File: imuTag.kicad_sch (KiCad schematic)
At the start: 33 parts, among them J1 Conn_02x05_Odd_Even, J2 Conn_01x04_Pin, J3 Conn_01x02_Pin, Q1 DMG2305UX-13, U1 E73-2G4M08S1C, U2 ME6211C30M5G-N, U3 GD25Q64ESIG, Y2 Crystal

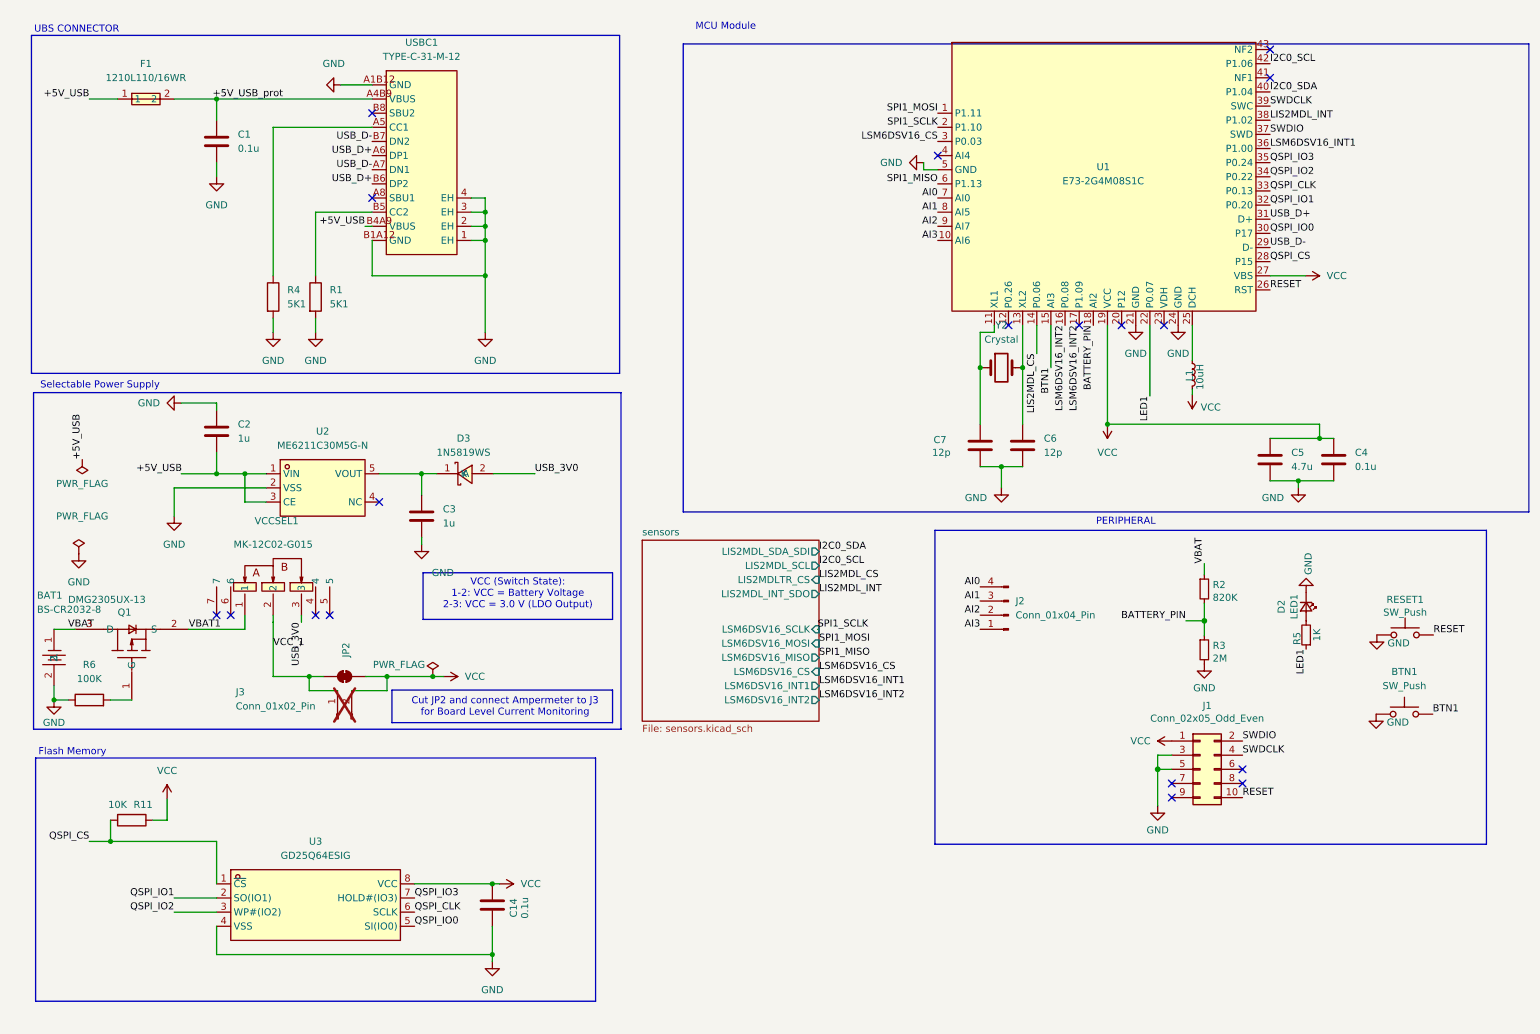
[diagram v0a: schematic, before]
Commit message: feat: imuTag mini PCBA v1.0 – initial release
PCB layout, schematics (imuTag + sensors), custom EasyEDA symbol/footprint libraries with 3D models, design rules, and production outputs (BOM, placement, netlist).
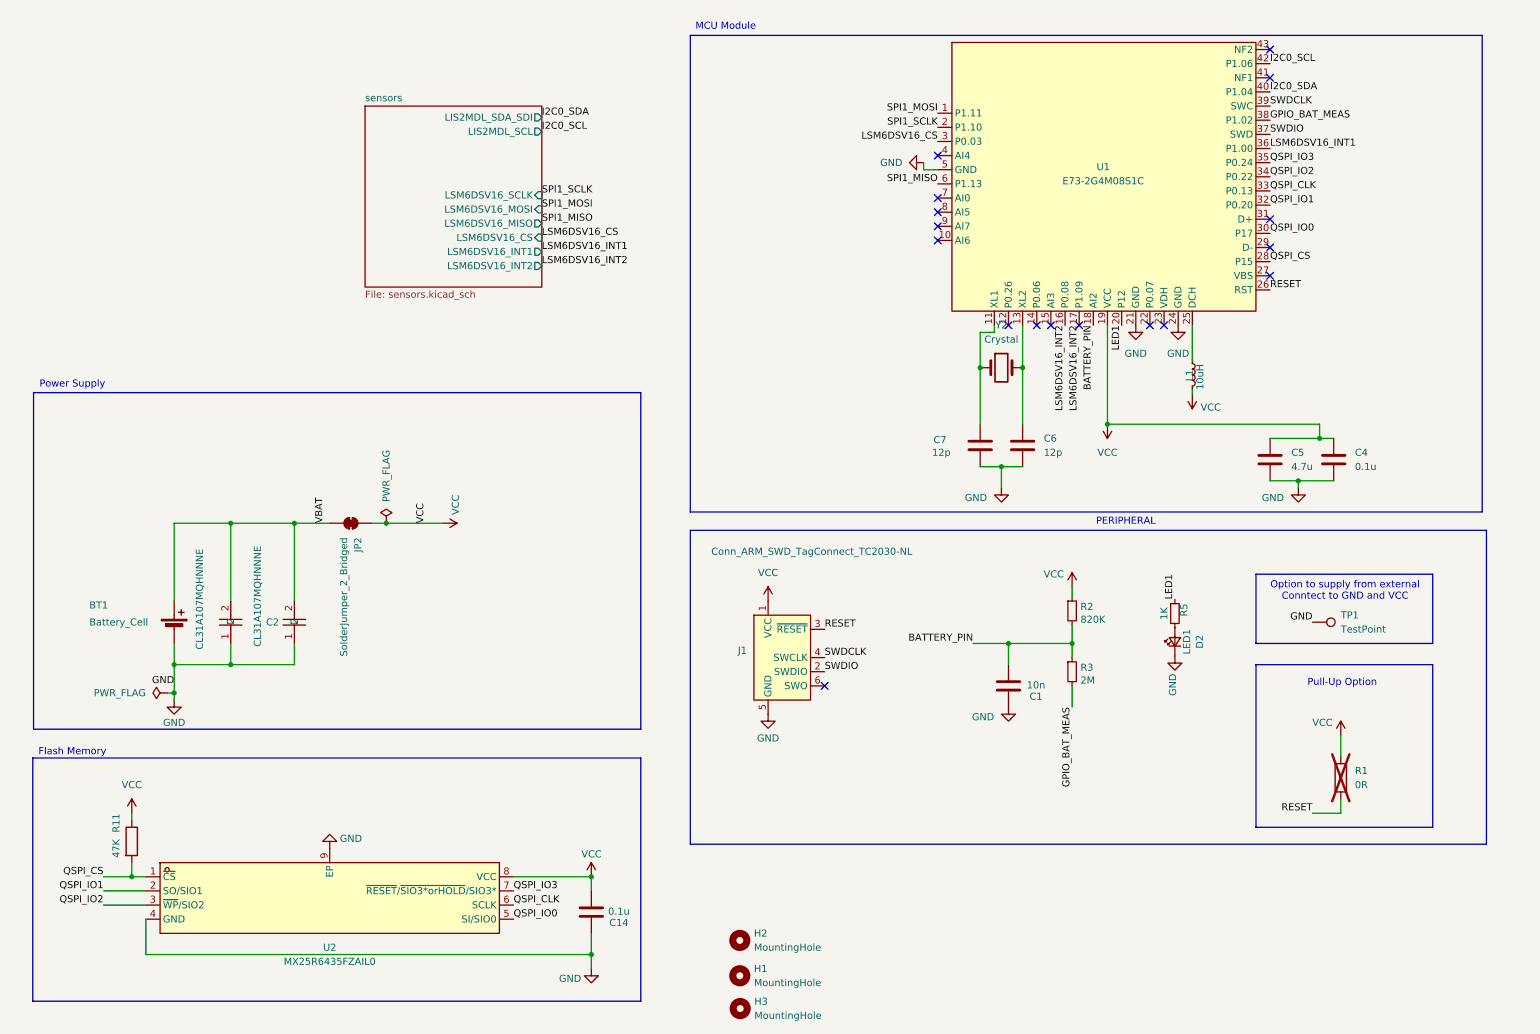
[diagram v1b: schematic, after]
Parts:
- removed BAT1: BS-CR2032-8, EasyEDA:BAT-TH_MY-2032-22, symbol EasyEDA:BS-CR2032-8
- removed BTN1, RESET1: SW_Push, EasyEDA:SW-SMD_TS-1086EV-AR03526, symbol Switch:SW_Push
- removed C2, C3: 1u, Capacitor_SMD:C_0603_1608Metric, symbol Device:C
- removed D3: 1N5819WS, EasyEDA:SOD-323_L1.8-W1.3-LS2.5-RD, symbol EasyEDA:1N5819WS
- removed F1: 1210L110/16WR, EasyEDA:F1210, symbol EasyEDA:1210L110_16WR
- removed J1: Conn_02x05_Odd_Even, Connector_PinHeader_1.27mm:PinHeader_2x05_P1.27mm_Vertical_SMD, symbol Connector_Generic:Conn_02x05_Odd_Even
- removed J2: Conn_01x04_Pin, Connector_PinHeader_2.54mm:PinHeader_1x04_P2.54mm_Vertical, symbol Connector:Conn_01x04_Pin
- removed J3: Conn_01x02_Pin, Connector_PinSocket_2.54mm:PinSocket_1x02_P2.54mm_Vertical, symbol Connector:Conn_01x02_Pin
- removed Q1: DMG2305UX-13, EasyEDA:SOT-23-3_L2.9-W1.3-P1.90-LS2.4-BR, symbol EasyEDA:DMG2305UX-13
- removed R4: 5K1, Resistor_SMD:R_0402_1005Metric, symbol Device:R
- removed R6: 100K, Resistor_SMD:R_0402_1005Metric, symbol Device:R
- removed U2: ME6211C30M5G-N, EasyEDA:SOT-23-5_L2.9-W1.6-P0.95-LS2.8-BL, symbol EasyEDA:ME6211C30M5G-N
- removed U3: GD25Q64ESIG, EasyEDA:SOP-8_L5.3-W5.3-P1.27-LS8.0-BL, symbol EasyEDA:GD25Q64ESIG
- removed USBC1: TYPE-C-31-M-12, EasyEDA:USB-C_SMD-TYPE-C-31-M-12_1, symbol EasyEDA:TYPE-C-31-M-12
- removed VCCSEL1: MK-12C02-G015, EasyEDA:SW-SMD_G-SWITCH_MK-12C02-G015, symbol EasyEDA:MK-12C02-G015
- added BT1: Battery_Cell, EasyEDA:CR2032_Custom_Contacts_SMD_AirTagStyle, symbol Device:Battery_Cell
- added C2, C8: CL31A107MQHNNNE, EasyEDA:C1206, symbol EASYEDA:CL31A107MQHNNNE
- added H1, H3: MountingHole, MountingHole:MountingHole_2.1mm, symbol Mechanical:MountingHole
- added H2: MountingHole, EasyEDA:Slot_1.2x3.0mm_NPTH, symbol Mechanical:MountingHole
- added J1: Conn_ARM_SWD_TagConnect_TC2030-NL, Connector:Tag-Connect_TC2030-IDC-NL_2x03_P1.27mm_Vertical, symbol Connector:Conn_ARM_SWD_TagConnect_TC2030-NL
- added TP1: TestPoint, TestPoint:TestPoint_Pad_D1.0mm, symbol Connector:TestPoint
- added U2: MX25R6435FZAIL0, EasyEDA:WSON-8_L4.0-W4.0-P0.80-BL-EP-1, symbol EasyEDA:MX25R6435FZAIL0
- C1: value 0.1u -> 10n
- JP2: footprint Jumper:SolderJumper-2_P1.3mm_Bridged_Pad1.0x1.5mm -> Jumper:SolderJumper-2_P1.3mm_Bridged2Bar_Pad1.0x1.5mm
- R1: value 5K1 -> 0R; footprint Resistor_SMD:R_0402_1005Metric -> Resistor_SMD:R_0805_2012Metric_Pad1.20x1.40mm_HandSolder; now not fitted
- R11: value 10K -> 47K
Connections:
- net +5V_USB_prot is gone; now on net GND: C1.1
- net VCC_1 is gone; now on net VCC: JP2.2 (B)
- net BATTERY_PIN: now also C1.2
- net GND: now also BT1.2 (-), C2.1, C8.1, J1.5 (GND), TP1.1, U2.4 (GND), U2.9 (EP); no longer C1.2, R1.2, R3.2
- net LED1: now also U1.20 (P12); no longer U1.22 (P0.07)
- net QSPI_CLK: now also U2.6 (SCLK)
- net QSPI_CS: now also U2.1 (~{CS})
- net QSPI_IO0: now also U2.5 (SI/SIO0)
- net QSPI_IO1: now also U2.2 (SO/SIO1)
- net QSPI_IO2: now also U2.3 (~{WP}/SIO2)
- net QSPI_IO3: now also U2.7 (~{RESET}/~{SIO3*orHOLD}/SIO3*)
- net RESET: now also R1.2, J1.3 (~{RESET})
- net SWDCLK: now also J1.4 (SWCLK)
- net SWDIO: now also J1.2 (SWDIO)
- net VBAT: now also JP2.1 (A), BT1.1 (+), C2.2, C8.2; no longer R2.1
- net VCC: now also R1.1, R2.1, J1.1 (VCC), U2.8 (VCC); no longer JP2.1 (A), U1.27 (VBS)
- net AI0: no longer names the net of U1.7 (AI0)
- net AI1: no longer names the net of U1.8 (AI5)
- net AI2: no longer names the net of U1.9 (AI7)
- net AI3: no longer names the net of U1.10 (AI6)
- net BTN1: no longer names the net of U1.15 (AI3)
- net LIS2MDL_CS: no longer names the net of U1.14 (P0.06)
- net LIS2MDL_INT renamed GPIO_BAT_MEAS
- net GPIO_BAT_MEAS: now also R3.2
- net USB_D+: no longer names the net of U1.31 (D+)
- net USB_D-: no longer names the net of U1.29 (D-)
- no-connect marks 18 -> 17
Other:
- sheet sensors ports: added none; removed LIS2MDLTR_CS, LIS2MDL_INT_SDO
- note added: "Option to supply from external Conntect to GND and VCC"
- note added: "Power Supply"
- note added: "Pull-Up Option"
- note removed: "Cut JP2 and connect Ampermeter to J3 for Board Level Current Monitoring"
- note removed: "Selectable Power Supply"
- note removed: "UBS CONNECTOR"
- note removed: "VCC (Switch State): 1-2: VCC = Battery Voltage 2-3: VCC = 3.0 V (LDO Output)"
- moved on the sheet: C14, D2, R11, R2, R3, R5

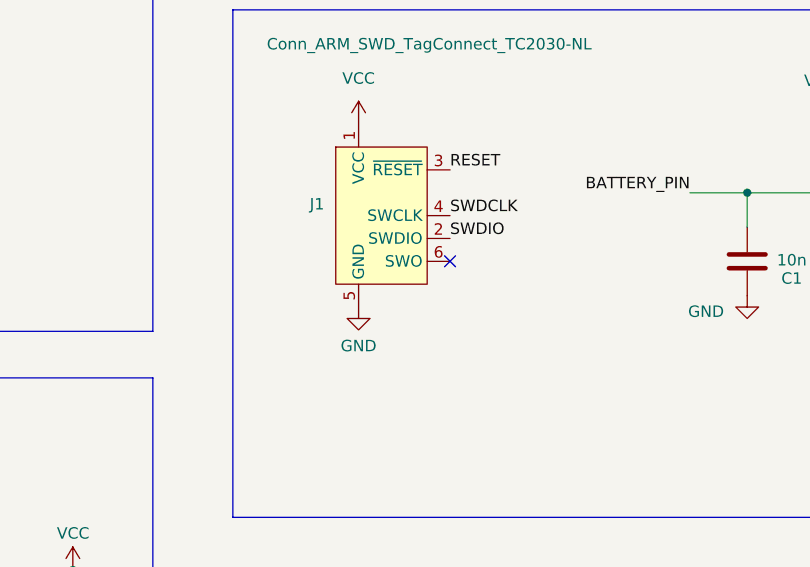
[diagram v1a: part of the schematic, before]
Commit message: fix: wire unconnected pin and clear DRC exclusions
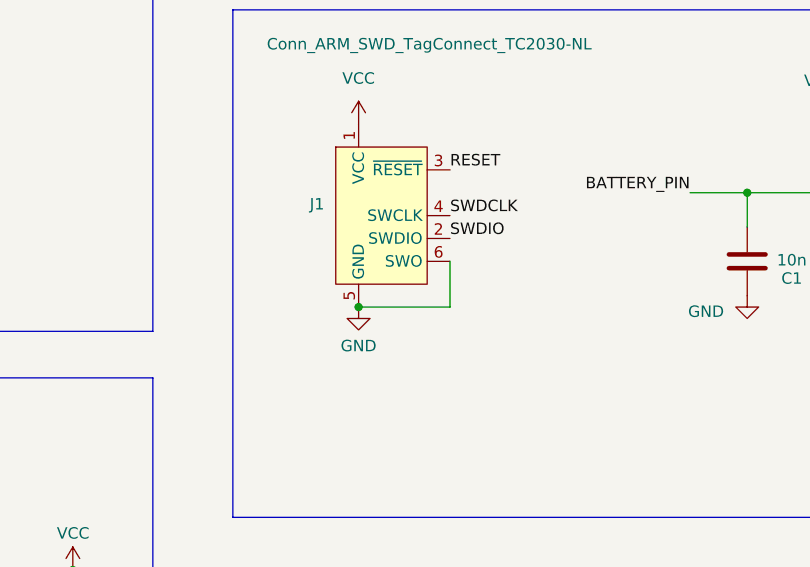
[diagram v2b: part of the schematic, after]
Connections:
- net GND: now also J1.6 (SWO)
- no-connect marks 17 -> 16
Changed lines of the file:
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@@
+	)
+	(junction
+		(at 149.86 139.7)
+		(diameter 0)
+		(color 0 0 0 0)
 	)
 	(junction
@@
 	)
 	(no_connect
-		(at 160.02 134.62)
-	)
-	(no_connect
 		(at 220.98 69.85)
 	)
@@
 	(wire
 		(pts
+			(xy 160.02 134.62) (xy 160.02 139.7)
+		)
+		(stroke
+			(width 0)
+			(type default)
+		)
+	)
+	(wire
+		(pts
 			(xy 210.82 87.63) (xy 210.82 69.85)
 		)
@@
 		)
 		(stroke
+			(width 0)
+			(type default)
+		)
+	)
+	(wire
+		(pts
+			(xy 160.02 139.7) (xy 149.86 139.7)
+		)
+		(stroke

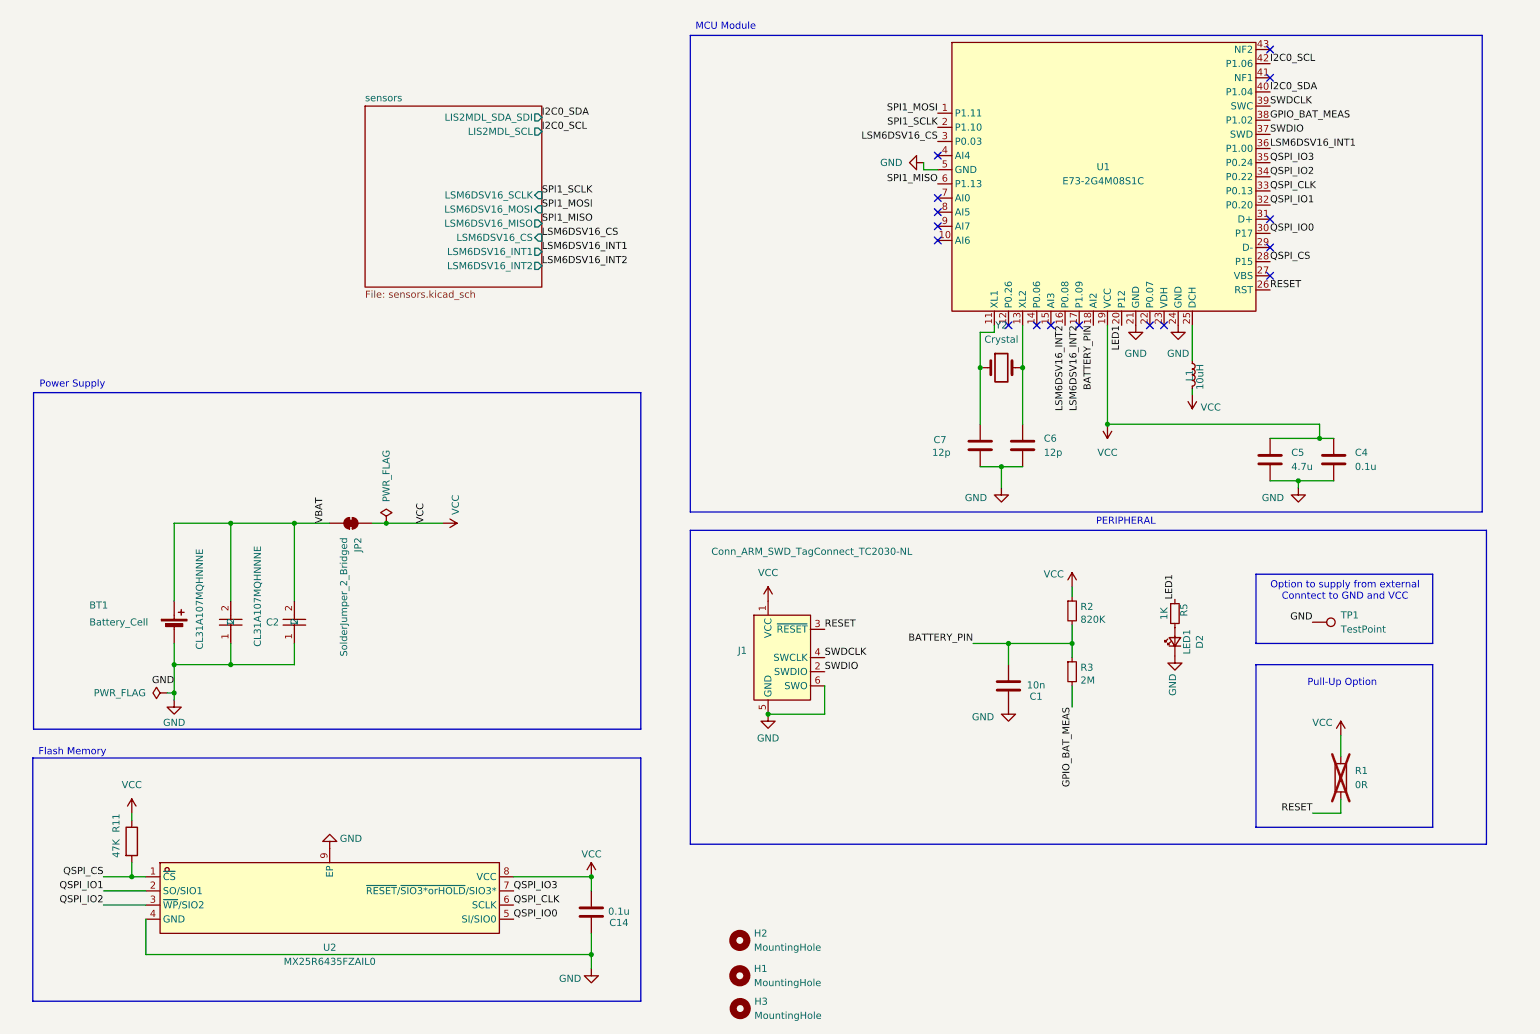
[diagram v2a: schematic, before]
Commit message: feat: add NFC antenna support via E73-2G4M08S1C
- Add NFC matching network (ESD protection, 100pF tuning caps)
- Add hybrid antenna connector (JST SH 1.0mm + hand-solder test pads)
- Add 4-layer keepout zones around NFC traces and antenna feed
- Route and length-balance NFC1/NFC2 traces
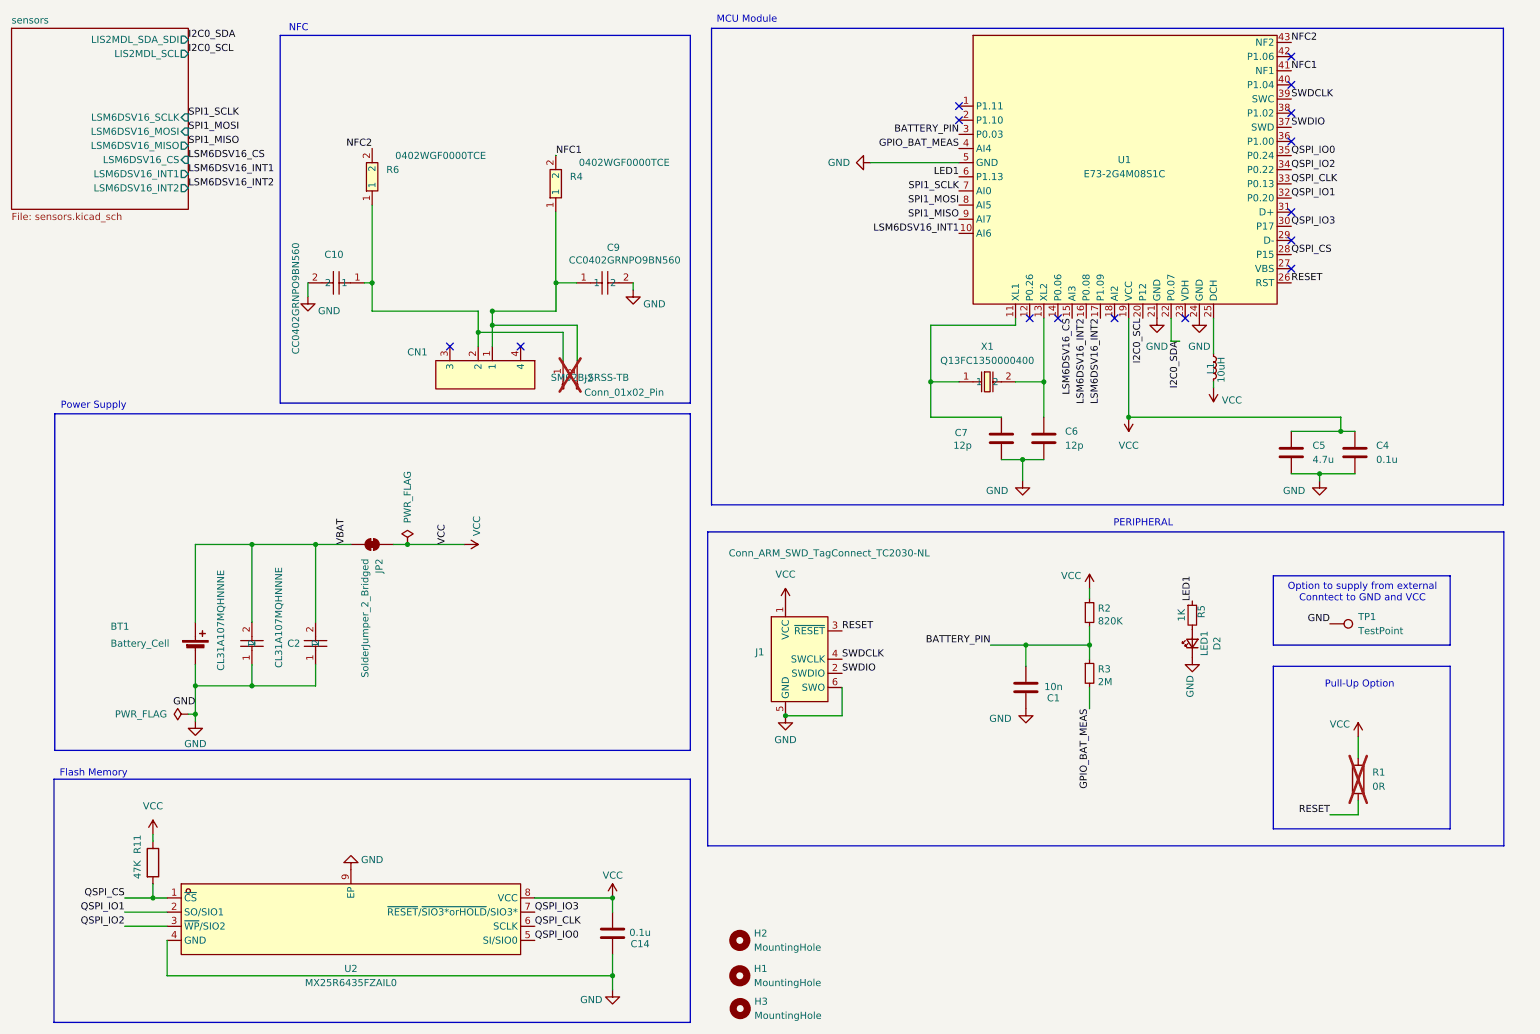
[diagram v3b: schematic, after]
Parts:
- removed Y2: Crystal, Crystal:Crystal_SMD_3215-2Pin_3.2x1.5mm, symbol Device:Crystal
- added C10, C9: CC0402GRNPO9BN560, EasyEDA:C0402, symbol EasyEDA:CC0402GRNPO9BN560
- added CN1: SM02B-SRSS-TB, EasyEDA:CONN-SMD_2P-P1.00_SM02B-SRSS-TB-LF-SN, symbol EASYEDA:SM02B-SRSS-TB
- added J2: Conn_01x02_Pin, Connector_PinHeader_1.27mm:PinHeader_1x02_P1.27mm_Vertical, symbol Connector:Conn_01x02_Pin
- added R4: 0402WGF0000TCE, Resistor_SMD:R_0402_1005Metric, symbol EASYEDA:0402WGF0000TCE
- added R6: 0402WGF0000TCE, EasyEDA:R0402, symbol EASYEDA:0402WGF0000TCE
- added X1: Q13FC1350000400, EasyEDA:FC-135R_L3.2-W1.5, symbol EASYEDA:Q13FC1350000400
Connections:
- net BATTERY_PIN: now also U1.3 (P0.03); no longer U1.18 (AI2)
- net GND: now also C10.2, C9.2
- net GPIO_BAT_MEAS: now also U1.4 (AI4); no longer U1.38 (P1.02)
- net I2C0_SCL: now also U1.20 (P12); no longer U1.42 (P1.06)
- net I2C0_SDA: now also U1.22 (P0.07); no longer U1.40 (P1.04)
- net LED1: now also U1.6 (P1.13); no longer U1.20 (P12)
- net LSM6DSV16_CS: now also U1.15 (AI3); no longer U1.3 (P0.03)
- net LSM6DSV16_INT1: now also U1.10 (AI6); no longer U1.36 (P1.00)
- net QSPI_IO0: now also U1.35 (P0.24); no longer U1.30 (P17)
- net QSPI_IO3: now also U1.30 (P17); no longer U1.35 (P0.24)
- net SPI1_MISO: now also U1.9 (AI7); no longer U1.6 (P1.13)
- net SPI1_MOSI: now also U1.8 (AI5); no longer U1.1 (P1.11)
- net SPI1_SCLK: now also U1.7 (AI0); no longer U1.2 (P1.10)
- net at C7.1, U1.11 (XL1): now also X1.1
- net at C6.1, U1.13 (XL2): now also X1.2
- net NFC1: now reaches U1.41 (NF1)
- net NFC1: now also R4.2
- net NFC2: now reaches U1.43 (NF2)
- net NFC2: now also R6.2
- new net: C9.1, CN1.1, J2.2 (Pin_2), R4.1
- new net: C10.1, CN1.2, J2.1 (Pin_1), R6.1
- no-connect marks 16 -> 15
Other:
- note added: "NFC"
- moved on the sheet: BT1, C1, C14, C2, C4, C5, C6, C7, D2, J1, JP2, L1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
